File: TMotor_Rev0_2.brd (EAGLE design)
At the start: 106.7 x 74.3 mm, 94 parts, among them J1 5015680507, J10 5015680207, J2 5015680507, J7 5015680207, J8 5015680207, J9 5015680207, Q1 IRLB8721PBFTO220H, Q2 IRLB8721PBFTO220H, Q3 IRLB8721PBFTO220H, Q4 IRLB8721PBFTO220H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

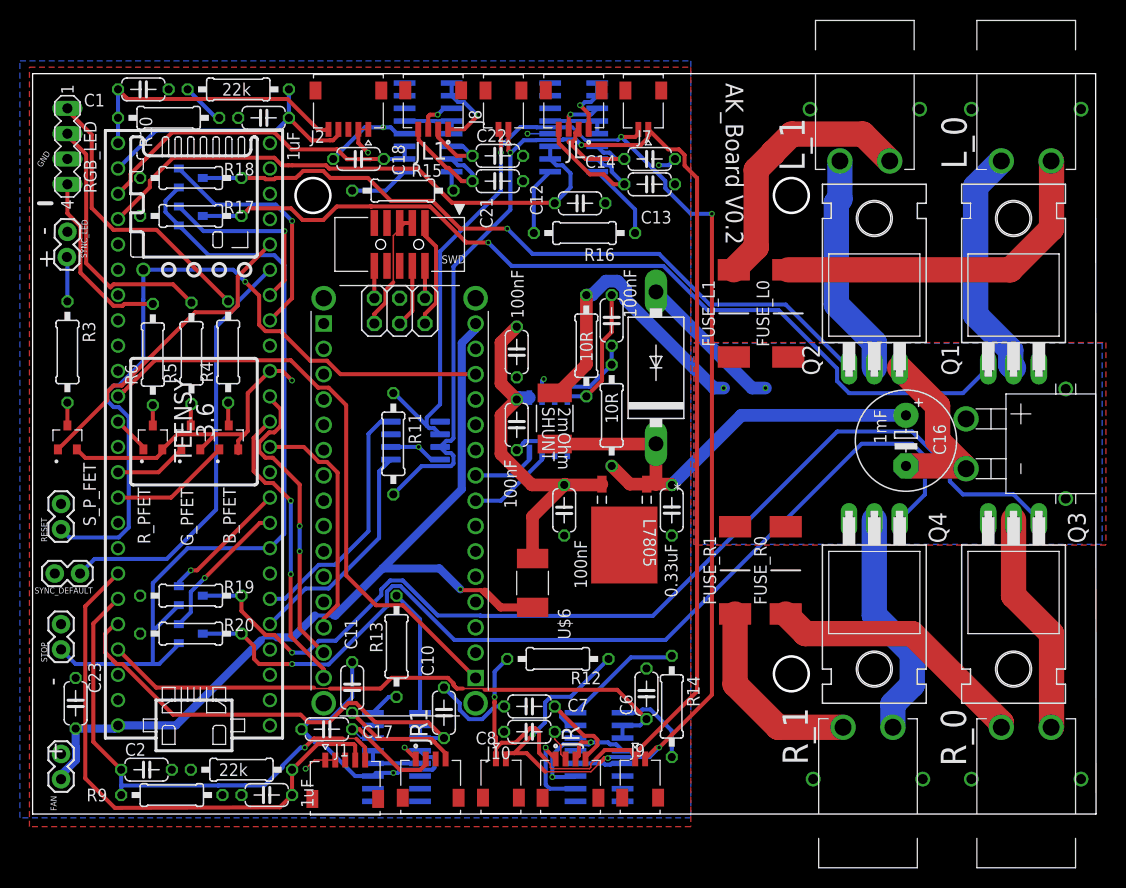
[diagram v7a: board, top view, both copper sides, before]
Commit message: Restricted area over CAN
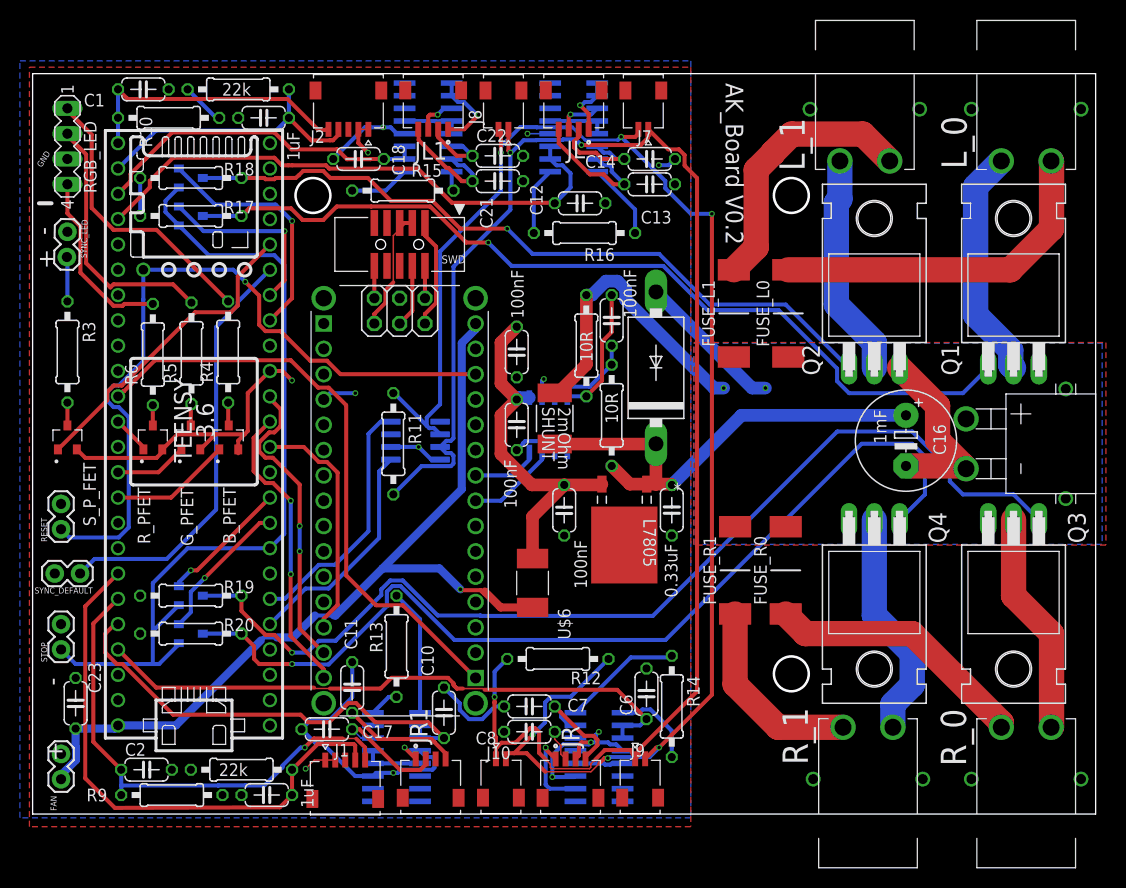
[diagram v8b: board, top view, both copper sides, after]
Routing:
- net GND: track 125.1 -> 133.6 mm, vias 11 -> 13
- net TRQ_AMP_R1: track 48.4 -> 46.4 mm
- net TRQ_AMP_R: track 61.9 -> 60.8 mm
- net N$10: track 11.5 -> 10.8 mm
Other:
- board text added: "1. Test with multiple motors running to make sure the sensors still work."
- board text added: "2. Pull up on reset"
- board text added: "3. Figure out how to keep SPI from preventing flashing"
- board text added: "4. Remove battery monitor and shift to boost circuit and conver to inspired Energy battery"
- board text removed: "1."
- board text removed: "2."
- board text removed: "3."
- board text removed: "4."
